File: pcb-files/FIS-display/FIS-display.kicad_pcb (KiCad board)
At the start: 2 copper layers, 69.6 x 79.5 mm, 31 parts, among them J1 Conn_01x03_Pin, J2 Conn_01x03_Socket, J3 Conn_01x02_Socket, Q1 BS170, Q2 BS170, Q3 BS170, Q4 BS170, Q5 BS170, Q6 BS170, U2 MCP2561-H-P

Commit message: PCB: update KiCad design and Gerbers; add design backups
Made-with: Cursor
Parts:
- J1: footprint Connector_JST:JST_PH_B3B-PH-K_1x03_P2.00mm_Vertical -> Connector_PinHeader_2.54mm:PinHeader_1x03_P2.54mm_Vertical
- J2: value Conn_01x03_Socket -> Conn_01x03_Pin; footprint Connector_JST:JST_PH_B3B-PH-K_1x03_P2.00mm_Vertical -> Connector_PinHeader_2.54mm:PinHeader_1x03_P2.54mm_Vertical
- moved J2 3.21 mm to (156.8, 65.1), turned to 90 degrees
- moved J1 3.04 mm to (110.6, 64.6), turned to 90 degrees
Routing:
- net 3.3VDC: track 158.2 -> 174.7 mm
- net FIS_PIN_CLK : track 77.8 -> 66.6 mm, vias 1 -> 2
- net FIS_CAN_  RXCAN: track 46.7 -> 38.7 mm, vias 2 -> 0
- net VDD: track 171.8 -> 164.1 mm
- net FIS_PIN_ENA_OUT: track 35.1 -> 30.5 mm, vias 1 -> 0
- net Net-(J3-Pin_2): track 28.5 -> 26.9 mm, vias 0 -> 1
- net FIS_PIN_ENA: track 57.0 -> 58.6 mm
- net TX_CLK: track 29.8 -> 31.2 mm
- net RX_ENA: track 21.0 -> 19.7 mm
- net FIS_PIN_CLK_OUT : track 41.9 -> 40.9 mm, vias 1 -> 0
- net RX_CLK: track 33.9 -> 33.1 mm
- net TX_ENA: track 19.4 -> 20.1 mm, vias 0 -> 1
- net FIS_CAN_TXCAN: track 35.6 -> 36.3 mm
- net TX_DATA: track 43.5 -> 43.0 mm
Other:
- board text added: "1"

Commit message: README: add PCB 3D image; update PCB/KiCad and Gerbers
Made-with: Cursor
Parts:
- added J4: Conn_01x14_Pin, Connector_PinHeader_2.54mm:PinHeader_1x14_P2.54mm_Vertical, F.Cu at (119.6, 124.9)
- moved J3 22.5 mm to (121.8, 108.6)
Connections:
- A1 pad 21: unconnected-(A1-GPIO16-Pad21) -> CS
- A1 pad 22: unconnected-(A1-GPIO17-Pad22)_1 -> RESET
- A1 pad 24: unconnected-(A1-GPIO18-Pad24)_1 -> DC/RS
- A1 pad 25: unconnected-(A1-GPIO19-Pad25) -> SDI
- A1 pad 26: unconnected-(A1-GPIO20-Pad26) -> SCK
- A1 pad 27: unconnected-(A1-GPIO21-Pad27) -> LED
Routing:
- net SCK: track 0.00 -> 54.4 mm, vias 0 -> 2
- net LED: track 0.00 -> 49.4 mm
- net SDI: track 0.00 -> 48.1 mm, vias 0 -> 2
- net CS: track 0.00 -> 43.6 mm, vias 0 -> 1
- net DC/RS: track 0.00 -> 42.2 mm, vias 0 -> 1
- net RESET: track 0.00 -> 41.3 mm, vias 0 -> 1
- net FIS_PIN_CLK_OUT : track 40.9 -> 58.8 mm
- net 3.3VDC: track 174.7 -> 188.2 mm, vias 1 -> 0
- net FIS_PIN_ENA: track 58.6 -> 47.9 mm, vias 1 -> 0
- net FIS_PIN_DATA_OUT: track 56.7 -> 48.6 mm
- net Net-(J3-Pin_2): track 26.9 -> 18.9 mm, vias 1 -> 0
- net Net-(J3-Pin_1): track 29.9 -> 23.7 mm
- net FIS_PIN_ENA_OUT: track 30.5 -> 35.2 mm, vias 0 -> 1
- net FIS_PIN_DATA: track 72.1 -> 67.9 mm
- net RX_ENA: track 19.7 -> 22.7 mm, vias 0 -> 1
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
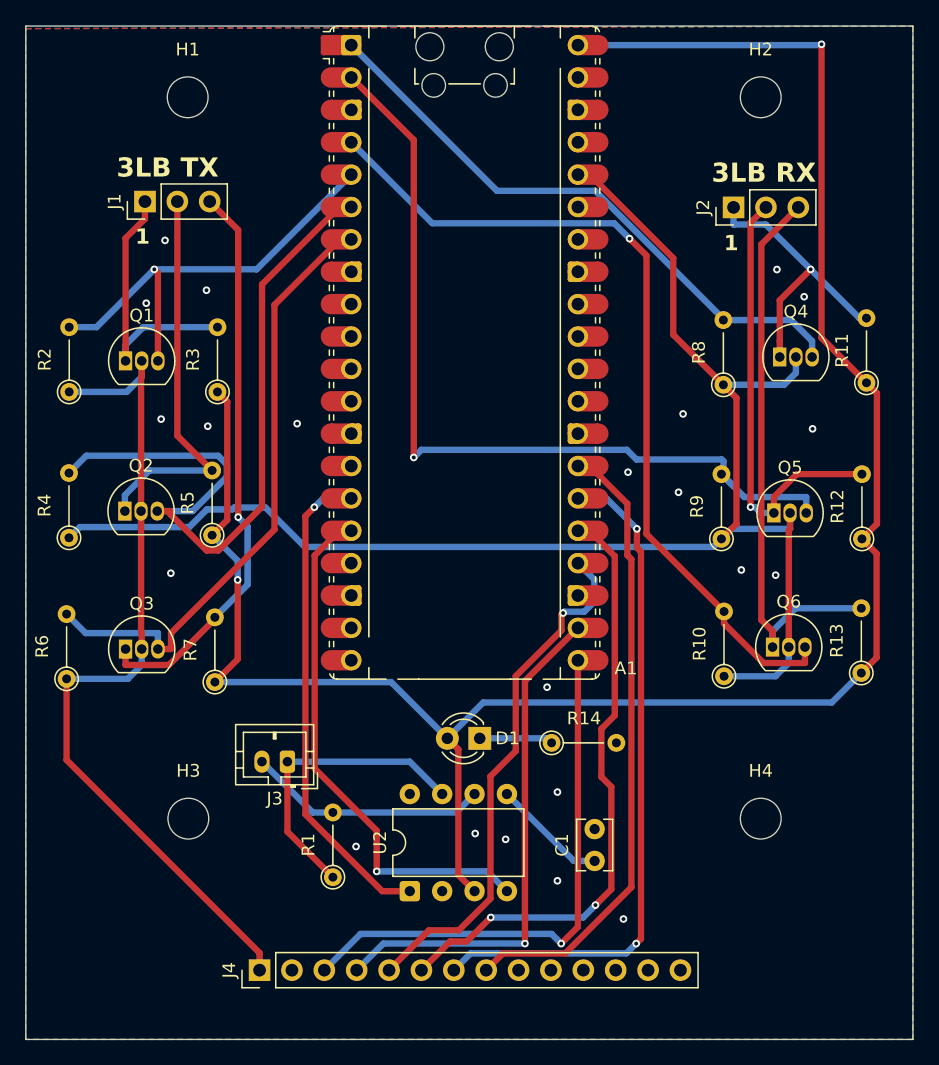
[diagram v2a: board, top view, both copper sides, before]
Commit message: README: section 10 formatting, LCD wiki/driver refs, ILI9341 window addressing; PCB/KiCad/PDF/Gerbers
Made-with: Cursor
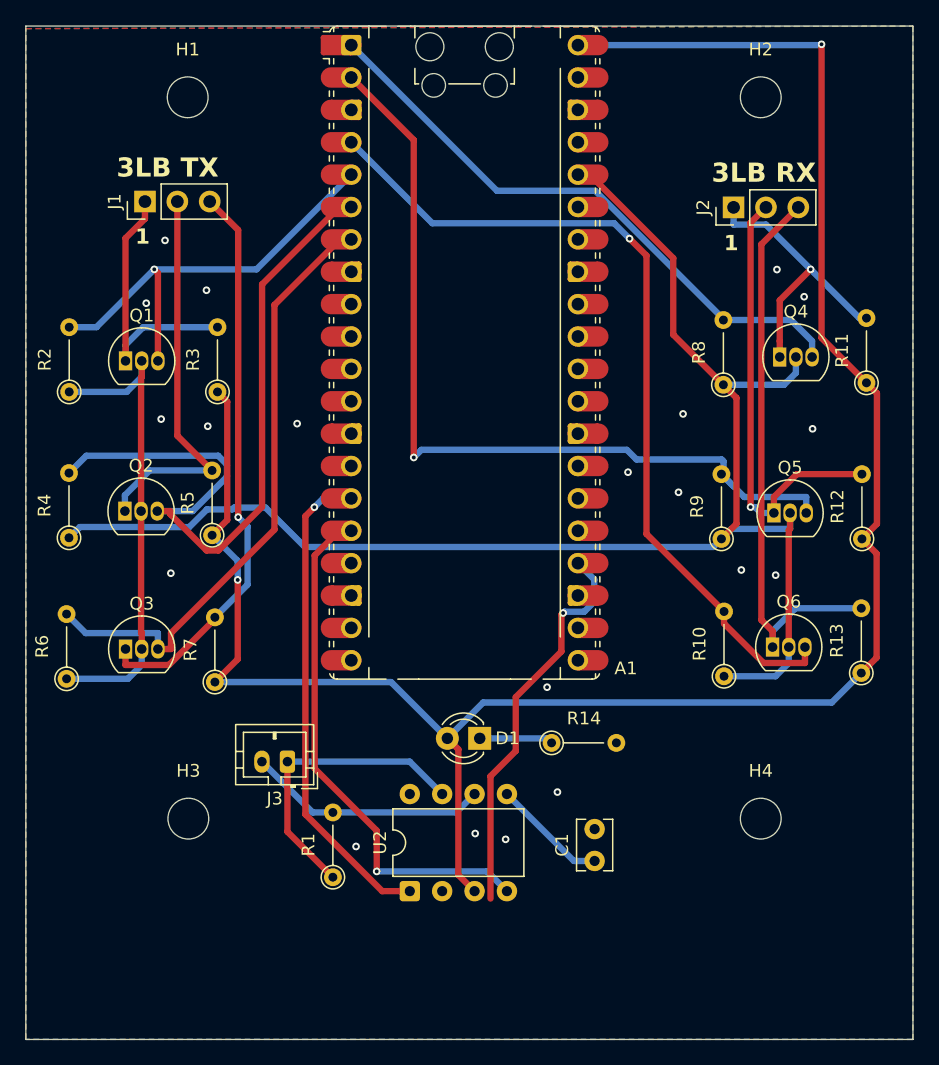
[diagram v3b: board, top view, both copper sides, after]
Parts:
- removed J4: Conn_01x14_Pin, Connector_PinHeader_2.54mm:PinHeader_1x14_P2.54mm_Vertical
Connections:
- A1 pad 21: CS -> unconnected-(A1-GPIO16-Pad21)
- A1 pad 22: RESET -> unconnected-(A1-GPIO17-Pad22)_1
- A1 pad 24: DC/RS -> unconnected-(A1-GPIO18-Pad24)_1
- A1 pad 25: SDI -> unconnected-(A1-GPIO19-Pad25)
- A1 pad 26: SCK -> unconnected-(A1-GPIO20-Pad26)
- A1 pad 27: LED -> unconnected-(A1-GPIO21-Pad27)
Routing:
- net SCK: track 54.4 -> 0.00 mm, vias 2 -> 0
- net LED: track 49.4 -> 0.00 mm
- net SDI: track 48.1 -> 0.00 mm, vias 2 -> 0
- net CS: track 43.6 -> 0.00 mm, vias 1 -> 0
- net DC/RS: track 42.2 -> 0.00 mm, vias 1 -> 0
- net RESET: track 41.3 -> 0.00 mm, vias 1 -> 0
- net (no net): track 0.00 -> 36.1 mm, vias 0 -> 1
- net 3.3VDC: track 188.2 -> 159.0 mm
- net GND: vias 22 -> 20
